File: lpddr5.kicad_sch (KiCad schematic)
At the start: 38 parts, among them U1 MT62F1G32D4DR-031_WT:B

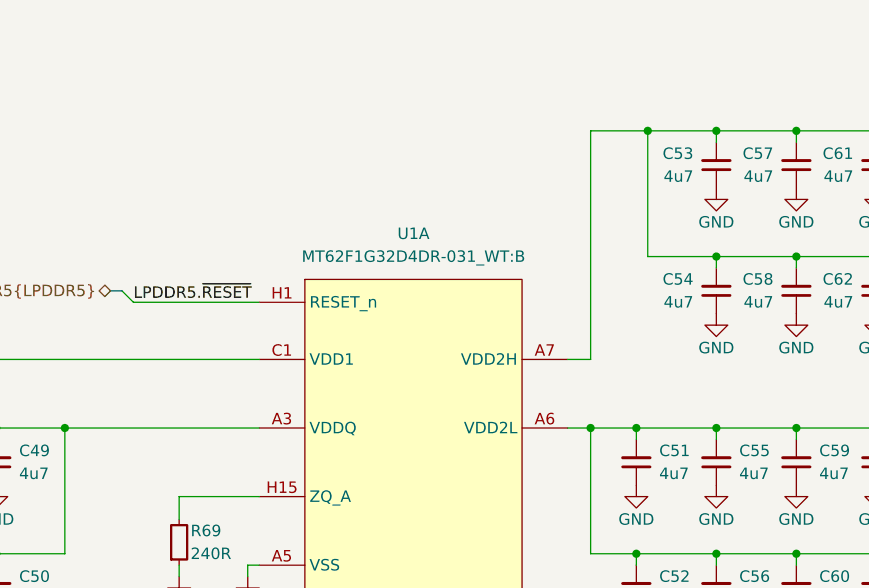
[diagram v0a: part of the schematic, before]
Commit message: [#52835] schematics: add nominal rails voltage to lpddr5
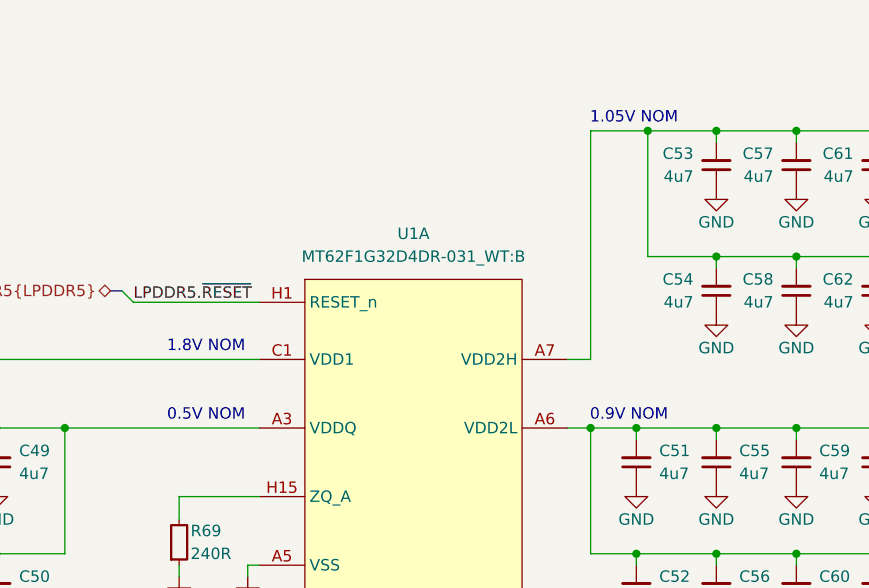
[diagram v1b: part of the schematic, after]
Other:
- note added: "0.5V NOM"
- note added: "0.9V NOM"
- note added: "1.05V NOM"
- note added: "1.8V NOM"
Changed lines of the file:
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@@
     )
+  )
+  (text " 0.5V NOM" (at 168.275 66.675 0)
+    (effects (font (size 1.27 1.27)) (justify left bottom))
+  )
+  (text " 0.9V NOM" (at 215.265 66.675 0)
+    (effects (font (size 1.27 1.27)) (justify left bottom))
+  )
+  (text " 1.05V NOM" (at 215.265 33.655 0)
+    (effects (font (size 1.27 1.27)) (justify left bottom))
   )
   (text "TODO: check what to do with unconnected" (at 236.22 203.2 0)
@@
     (effects (font (size 2.4892 2.4892) (thickness 0.4978) bold) (justify left bottom))
   )
+  (text " 1.8V NOM" (at 168.275 59.055 0)
+    (effects (font (size 1.27 1.27)) (justify left bottom))
+  )
   (label "LPDDR5.WCK_A_0_P" (at 74.93 157.48 0)

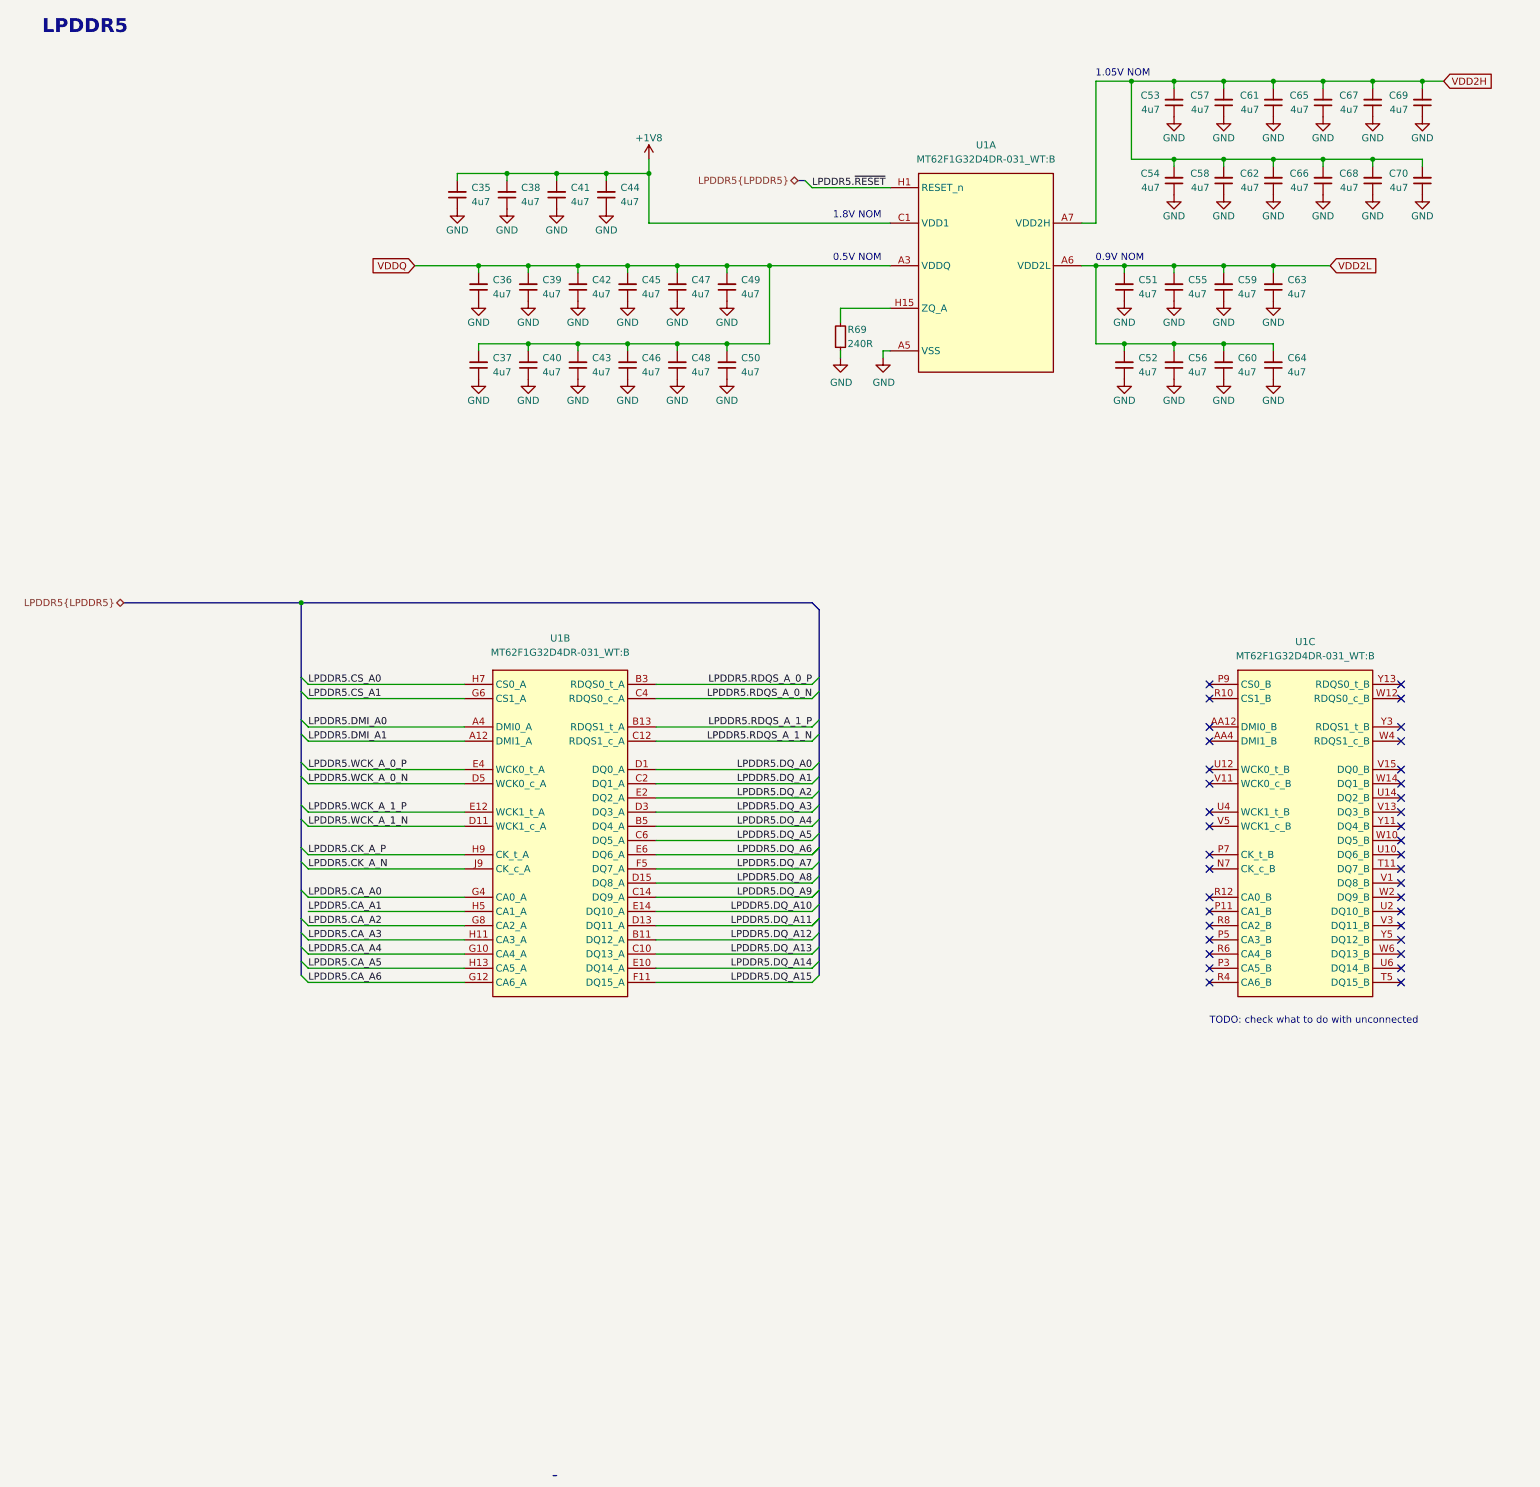
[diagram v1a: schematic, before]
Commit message: [#52835] schematics: update LPDDR5 connections, finish translators subsheet
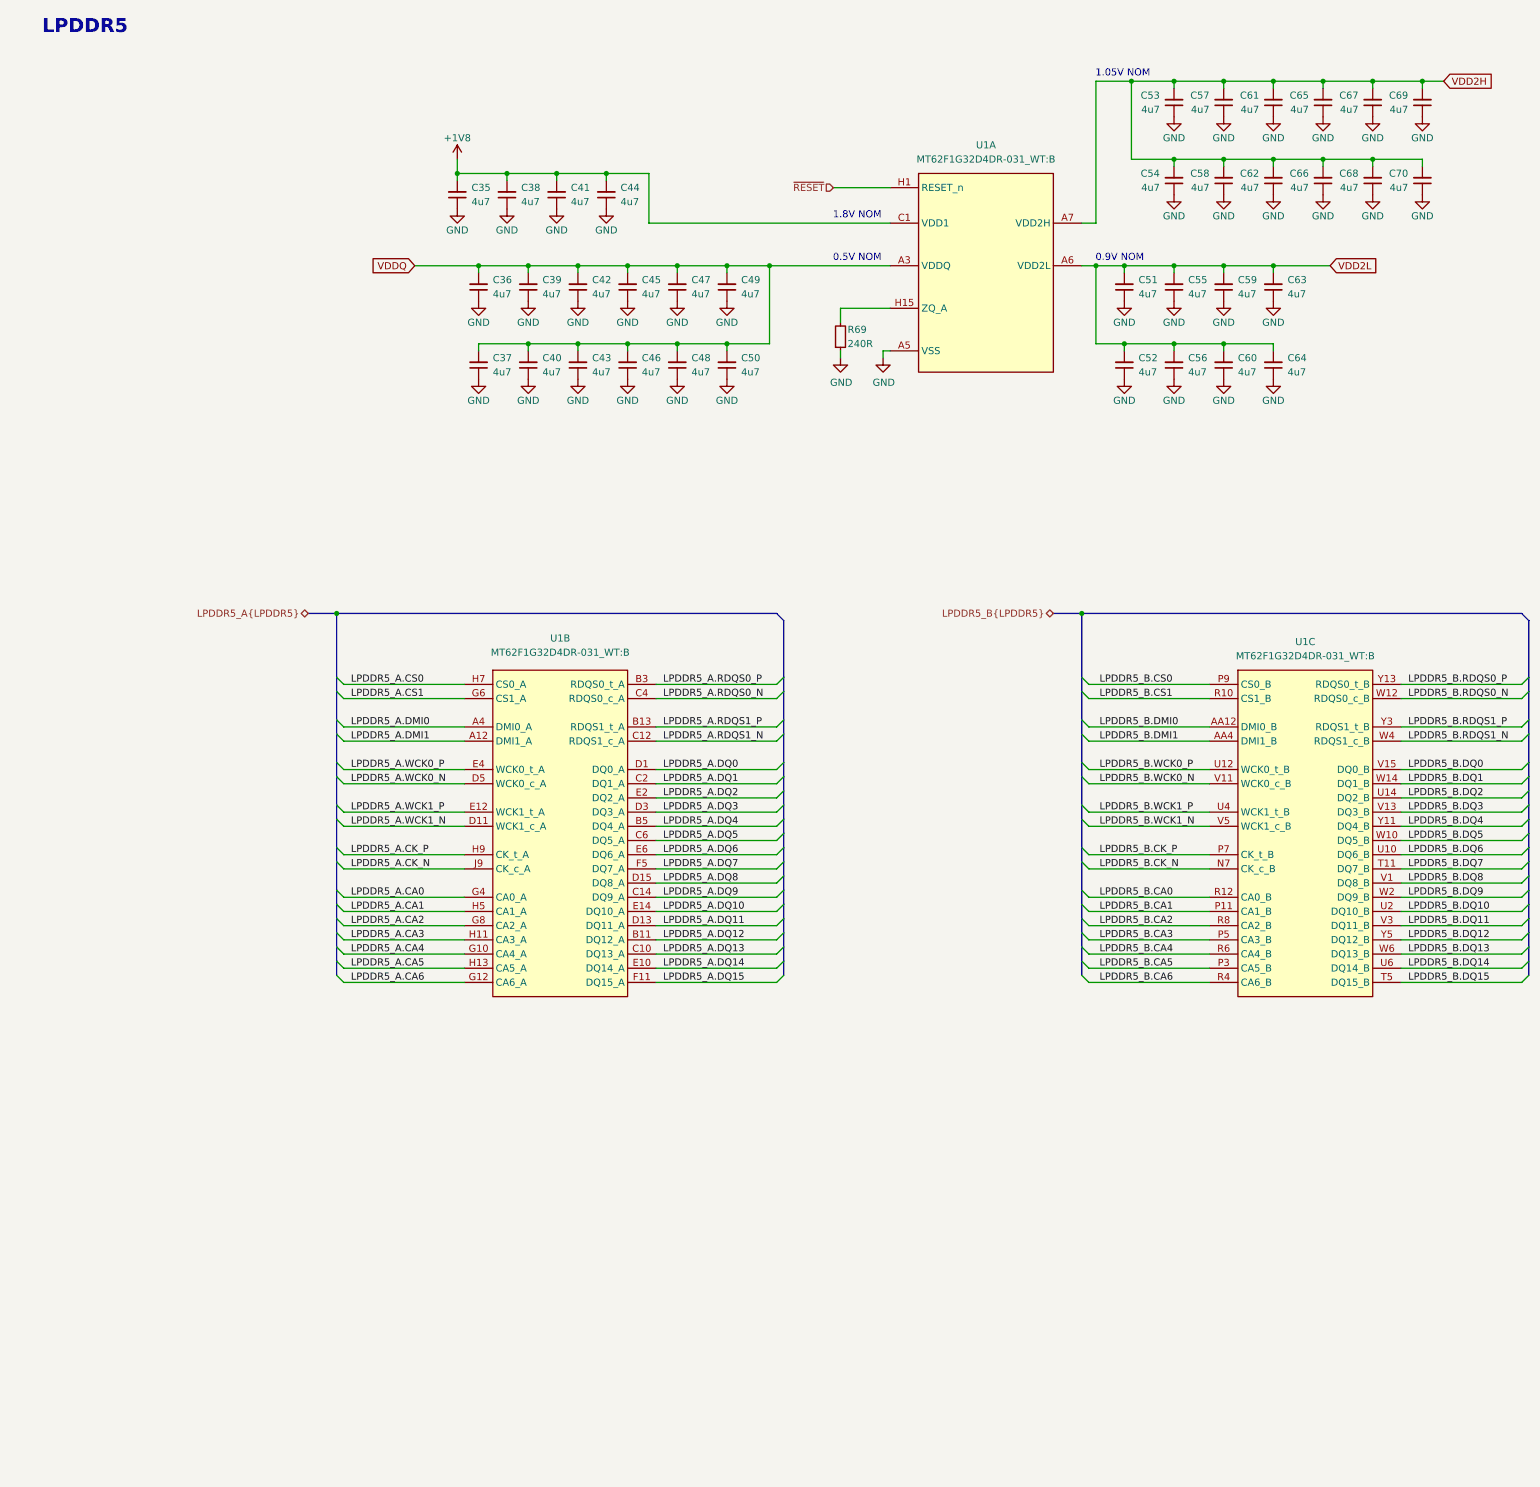
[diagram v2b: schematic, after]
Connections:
- net LPDDR5_B.DMI0: now reaches U1.AA12 (DMI0_B)
- net LPDDR5_B.DMI1: now reaches U1.AA4 (DMI1_B)
- net LPDDR5_B.CK_N: now reaches U1.N7 (CK_c_B)
- net LPDDR5_B.CA1: now reaches U1.P11 (CA1_B)
- net LPDDR5_B.CA5: now reaches U1.P3 (CA5_B)
- net LPDDR5_B.CA3: now reaches U1.P5 (CA3_B)
- net LPDDR5_B.CK_P: now reaches U1.P7 (CK_t_B)
- net LPDDR5_B.CS0: now reaches U1.P9 (CS0_B)
- net LPDDR5_B.CS1: now reaches U1.R10 (CS1_B)
- net LPDDR5_B.CA0: now reaches U1.R12 (CA0_B)
- net LPDDR5_B.CA6: now reaches U1.R4 (CA6_B)
- net LPDDR5_B.CA4: now reaches U1.R6 (CA4_B)
- net LPDDR5_B.CA2: now reaches U1.R8 (CA2_B)
- net LPDDR5_B.DQ7: now reaches U1.T11 (DQ7_B)
- net LPDDR5_B.DQ15: now reaches U1.T5 (DQ15_B)
- net LPDDR5_B.DQ6: now reaches U1.U10 (DQ6_B)
- net LPDDR5_B.WCK0_P: now reaches U1.U12 (WCK0_t_B)
- net LPDDR5_B.DQ2: now reaches U1.U14 (DQ2_B)
- net LPDDR5_B.DQ10: now reaches U1.U2 (DQ10_B)
- net LPDDR5_B.WCK1_P: now reaches U1.U4 (WCK1_t_B)
- net LPDDR5_B.DQ14: now reaches U1.U6 (DQ14_B)
- net LPDDR5_B.DQ8: now reaches U1.V1 (DQ8_B)
- net LPDDR5_B.WCK0_N: now reaches U1.V11 (WCK0_c_B)
- net LPDDR5_B.DQ3: now reaches U1.V13 (DQ3_B)
- net LPDDR5_B.DQ0: now reaches U1.V15 (DQ0_B)
- net LPDDR5_B.DQ11: now reaches U1.V3 (DQ11_B)
- net LPDDR5_B.WCK1_N: now reaches U1.V5 (WCK1_c_B)
- net LPDDR5_B.DQ5: now reaches U1.W10 (DQ5_B)
- net LPDDR5_B.RDQS0_N: now reaches U1.W12 (RDQS0_c_B)
- net LPDDR5_B.DQ1: now reaches U1.W14 (DQ1_B)
- net LPDDR5_B.DQ9: now reaches U1.W2 (DQ9_B)
- net LPDDR5_B.RDQS1_N: now reaches U1.W4 (RDQS1_c_B)
- net LPDDR5_B.DQ13: now reaches U1.W6 (DQ13_B)
- net LPDDR5_B.DQ4: now reaches U1.Y11 (DQ4_B)
- net LPDDR5_B.RDQS0_P: now reaches U1.Y13 (RDQS0_t_B)
- net LPDDR5_B.RDQS1_P: now reaches U1.Y3 (RDQS1_t_B)
- net LPDDR5_B.DQ12: now reaches U1.Y5 (DQ12_B)
- net LPDDR5.CA_A0 renamed LPDDR5_A.CA0
- net LPDDR5.CA_A1 renamed LPDDR5_A.CA1
- net LPDDR5.CA_A2 renamed LPDDR5_A.CA2
- net LPDDR5.CA_A3 renamed LPDDR5_A.CA3
- net LPDDR5.CA_A4 renamed LPDDR5_A.CA4
- net LPDDR5.CA_A5 renamed LPDDR5_A.CA5
- net LPDDR5.CA_A6 renamed LPDDR5_A.CA6
- net LPDDR5.CK_A_N renamed LPDDR5_A.CK_N
- net LPDDR5.CK_A_P renamed LPDDR5_A.CK_P
- net LPDDR5.CS_A0 renamed LPDDR5_A.CS0
- net LPDDR5.CS_A1 renamed LPDDR5_A.CS1
- net LPDDR5.DMI_A0 renamed LPDDR5_A.DMI0
- net LPDDR5.DMI_A1 renamed LPDDR5_A.DMI1
- net LPDDR5.DQ_A0 renamed LPDDR5_A.DQ0
- net LPDDR5.DQ_A1 renamed LPDDR5_A.DQ1
- net LPDDR5.DQ_A10 renamed LPDDR5_A.DQ10
- net LPDDR5.DQ_A11 renamed LPDDR5_A.DQ11
- net LPDDR5.DQ_A12 renamed LPDDR5_A.DQ12
- net LPDDR5.DQ_A13 renamed LPDDR5_A.DQ13
- net LPDDR5.DQ_A14 renamed LPDDR5_A.DQ14
- net LPDDR5.DQ_A15 renamed LPDDR5_A.DQ15
- net LPDDR5.DQ_A2 renamed LPDDR5_A.DQ2
- net LPDDR5.DQ_A3 renamed LPDDR5_A.DQ3
- net LPDDR5.DQ_A4 renamed LPDDR5_A.DQ4
- net LPDDR5.DQ_A5 renamed LPDDR5_A.DQ5
- net LPDDR5.DQ_A6 renamed LPDDR5_A.DQ6
- net LPDDR5.DQ_A7 renamed LPDDR5_A.DQ7
- net LPDDR5.DQ_A8 renamed LPDDR5_A.DQ8
- net LPDDR5.DQ_A9 renamed LPDDR5_A.DQ9
- net LPDDR5.RDQS_A_0_N renamed LPDDR5_A.RDQS0_N
- net LPDDR5.RDQS_A_0_P renamed LPDDR5_A.RDQS0_P
- net LPDDR5.RDQS_A_1_N renamed LPDDR5_A.RDQS1_N
- net LPDDR5.RDQS_A_1_P renamed LPDDR5_A.RDQS1_P
- net LPDDR5.WCK_A_0_N renamed LPDDR5_A.WCK0_N
- net LPDDR5.WCK_A_0_P renamed LPDDR5_A.WCK0_P
- net LPDDR5.WCK_A_1_N renamed LPDDR5_A.WCK1_N
- net LPDDR5.WCK_A_1_P renamed LPDDR5_A.WCK1_P
- net LPDDR5.~{RESET} renamed ~{RESET}
- no-connect marks 37 -> 0
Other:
- note removed: "TODO: check what to do with unconnected"

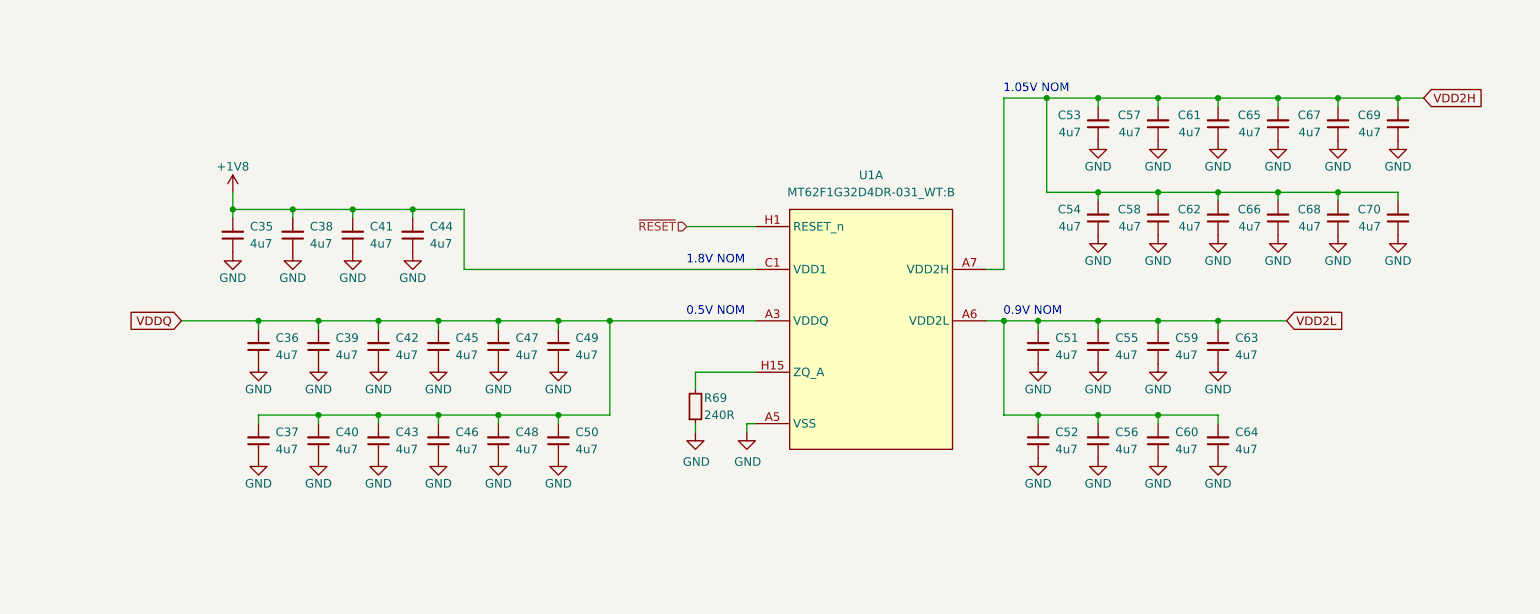
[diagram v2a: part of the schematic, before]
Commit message: [#52536] schematics: update I2C connection
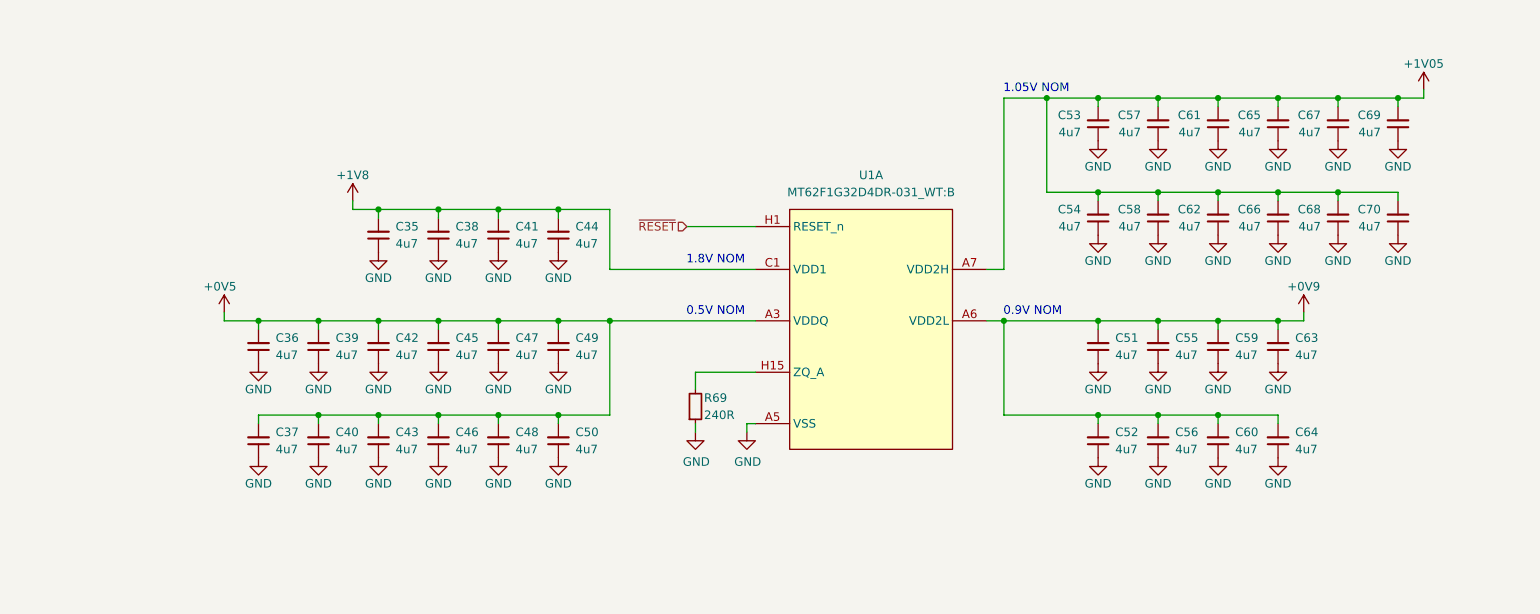
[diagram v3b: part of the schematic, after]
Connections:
- net VDD2H renamed +1V05
- net VDD2L renamed +0V9
- net VDDQ renamed +0V5
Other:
- moved on the sheet: C35, C38, C41, C44, C51, C52, C55, C56, C59, C60, C63, C64
